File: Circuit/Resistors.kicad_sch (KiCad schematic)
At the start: 23 parts, among them K3 AGQ200A12, K4 AGQ200A12, K5 AGQ200A12, K6 AGQ200A12, K7 AGQ200A12

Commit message: Output job, Revision Box and reorganise
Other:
- company: Harry and Yuki - EEE3 Instrumentation -> Harry Hill and Yuki Hoshino
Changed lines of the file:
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@@
 	(title_block
 		(title "Resistor Selector")
-		(date "2026-03-02")
+		(date "2026-05-02")
 		(rev "1.0")
-		(company "Harry and Yuki - EEE3 Instrumentation")
+		(company "Harry Hill and Yuki Hoshino")
+		(comment 1 "LCR Meter")
 	)
 	(text "fb=100k\n\n"

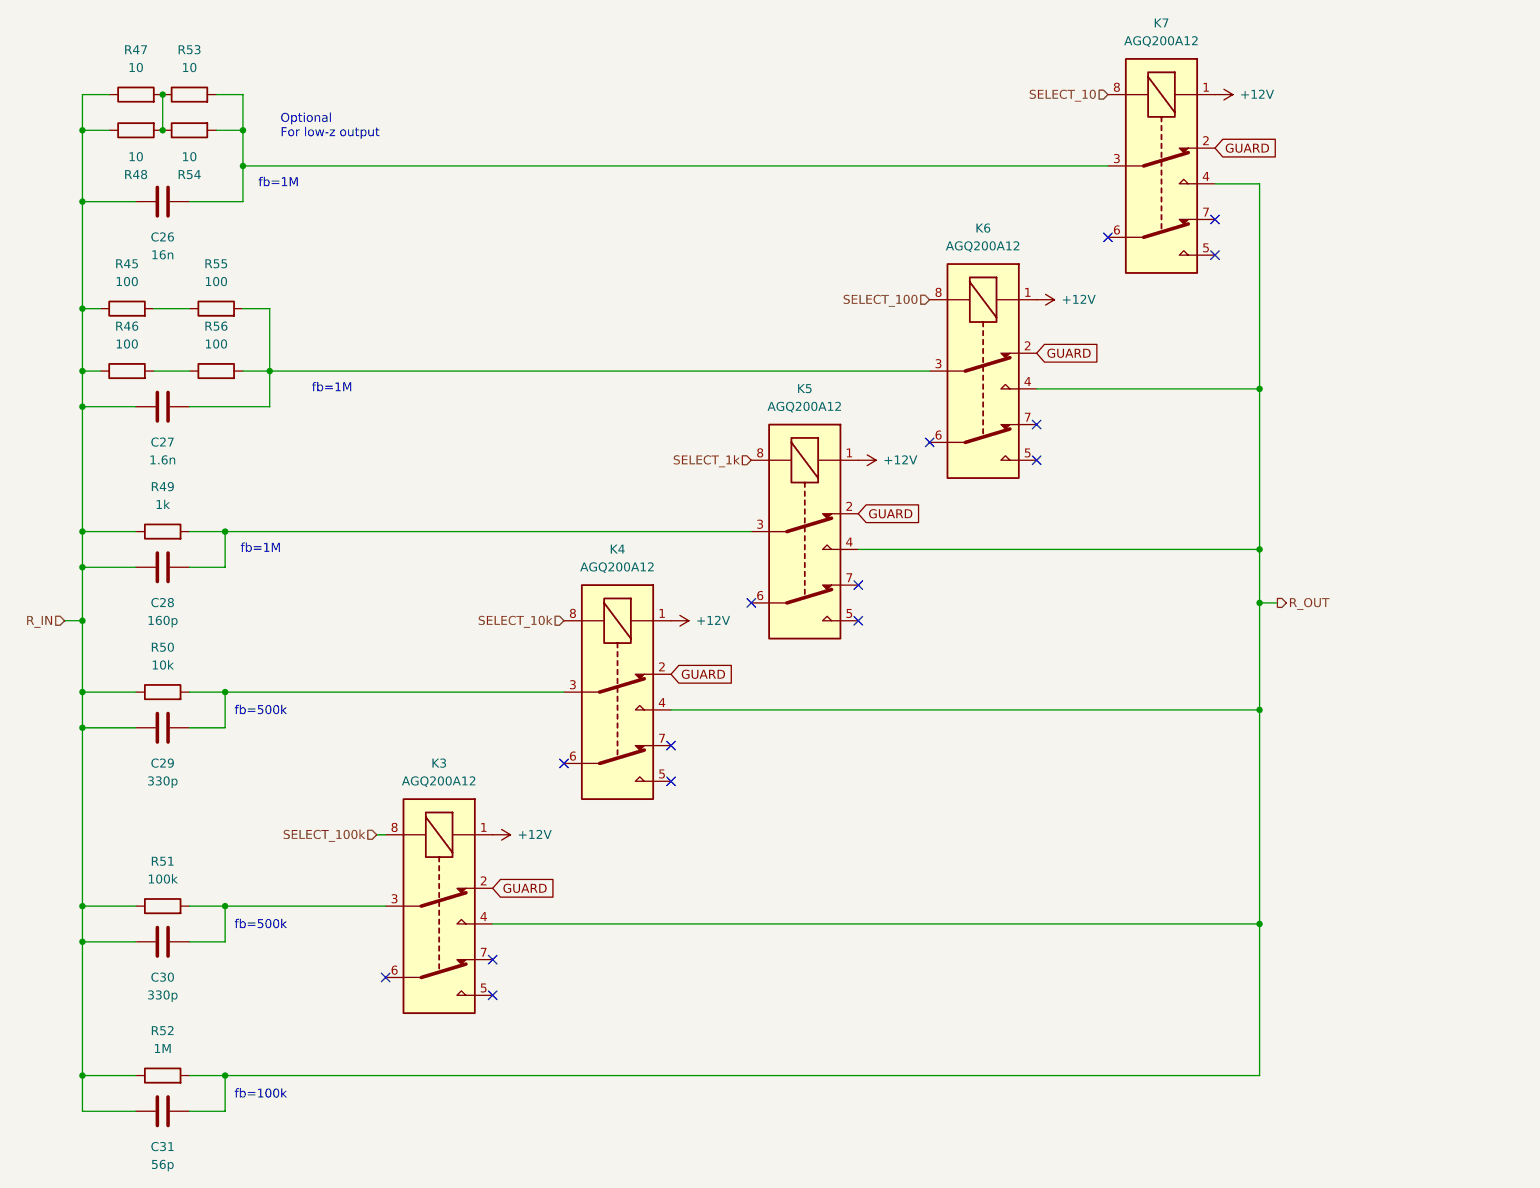
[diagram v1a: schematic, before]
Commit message: Input Protection Second Attempt
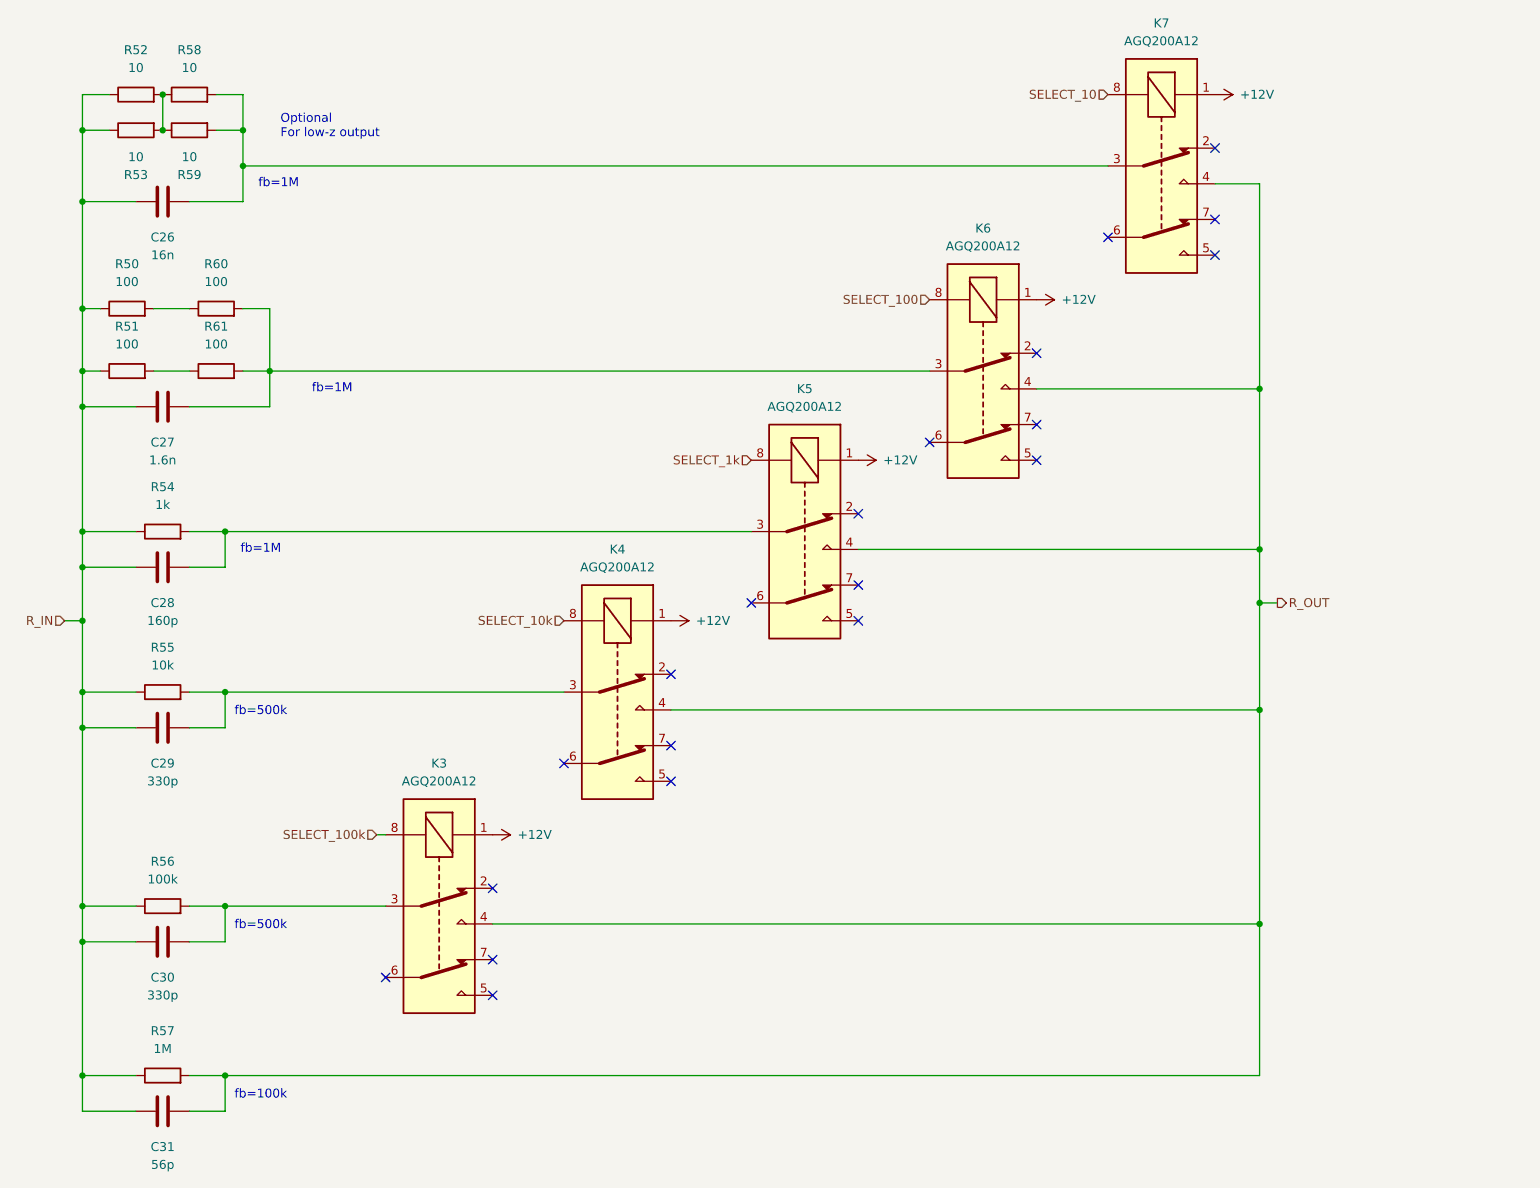
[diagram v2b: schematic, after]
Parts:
- renumbered R45 to R50, R46 to R51, R47 to R52, R48 to R53, R49 to R54, R50 to R55, R51 to R56, R52 to R57, R53 to R58, R54 to R59, R55 to R60, R56 to R61
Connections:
- removed net GUARD: K3.2, K4.2, K5.2, K6.2, K7.2
- no-connect marks 15 -> 20
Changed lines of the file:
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@@
 		(title "Resistor Selector")
 		(date "2026-05-02")
-		(rev "1.0")
+		(rev "0.1")
 		(company "Harry Hill and Yuki Hoshino")
 		(comment 1 "LCR Meter")
@@
 	)
 	(no_connect
+		(at 90.17 137.16)
+	)
+	(no_connect
 		(at 142.24 93.98)
 	)
@@
 	)
 	(no_connect
+		(at 142.24 83.82)
+	)
+	(no_connect
 		(at 167.64 76.2)
 	)
@@
 	)
 	(no_connect
+		(at 167.64 60.96)
+	)
+	(no_connect
 		(at 167.64 71.12)
 	)
@@
 	)
 	(no_connect
+		(at 193.04 31.75)
+	)
+	(no_connect
 		(at 177.8 44.45)
 	)
+	(no_connect
+		(at 115.57 106.68)
+	)
 	(wire
 		(pts
@@
 		)
 	)
-	(global_label "GUARD"
-		(shape input)
-		(at 115.57 106.68 0)
-		(fields_autoplaced yes)
-		(effects
-			(font
-				(size 1.27 1.27)
-			)
-			(justify left)
-		)
-		(property "Intersheetrefs" "${INTERSHEET_REFS}"
-			(at 124.7843 106.68 0)
-			(effects
-				(font
-					(size 1.27 1.27)
-				)
-				(justify left)
-				(hide yes)
-			)
-		)
-	)
-	(global_label "GUARD"
-		(shape input)
-		(at 142.24 83.82 0)
-		(fields_autoplaced yes)
-		(effects
-			(font
-				(size 1.27 1.27)
-			)
-			(justify left)
-		)
-		(property "Intersheetrefs" "${INTERSHEET_REFS}"
-			(at 151.4543 83.82 0)
-			(effects
-				(font
-					(size 1.27 1.27)
-				)
-				(justify left)
-				(hide yes)
-			)
-		)
-	)
-	(global_label "GUARD"
-		(shape input)
-		(at 167.64 60.96 0)
-		(fields_autoplaced yes)
-		(effects
-			(font
-				(size 1.27 1.27)
-			)
-			(justify left)
-		)
-		(property "Intersheetrefs" "${INTERSHEET_REFS}"
-			(at 176.8543 60.96 0)
-			(effects
-				(font
-					(size 1.27 1.27)
-				)
-				(justify left)
-				(hide yes)
-			)
-		)
-	)
-	(global_label "GUARD"
-		(shape input)
-		(at 193.04 31.75 0)
-		(fields_autoplaced yes)
-		(effects
-			(font
-				(size 1.27 1.27)
-			)
-			(justify left)
-		)
-		(property "Intersheetrefs" "${INTERSHEET_REFS}"
-			(at 202.2543 31.75 0)
-			(effects
-				(font
-					(size 1.27 1.27)
-				)
-				(justify left)
-				(hide yes)
-			)
-		)
-	)
-	(global_label "GUARD"
-		(shape input)
-		(at 90.17 137.16 0)
-		(fields_autoplaced yes)
-		(effects
-			(font
-				(size 1.27 1.27)
-			)
-			(justify left)
-		)
-		(property "Intersheetrefs" "${INTERSHEET_REFS}"
-			(at 99.3843 137.16 0)
-			(effects
-				(font
-					(size 1.27 1.27)
-				)
-				(justify left)
-				(hide yes)
-			)
-		)
-	)
 	(hierarchical_label "SELECT_10k"
 		(shape input)
@@
 		(dnp no)
 		(fields_autoplaced yes)
-		(property "Reference" "R49"
+		(property "Reference" "R54"
 			(at 43.18 80.01 90)
 			(effects
@@
 			(project "Main Board"
 				(path "/20aae4b7-3fb8-4924-82e8-1e7a29a313f8/6b7fef71-3444-4c8f-b2e2-502774ba9b51/2542314c-0b08-493b-856b-65d680d18812"
-					(reference "R49")
+					(reference "R54")
 					(unit 1)
 				)
@@
 		(dnp no)
 		(fields_autoplaced yes)
-		(property "Reference" "R47"
+		(property "Reference" "R52"
 			(at 39.37 17.78 90)
 			(effects
@@
 			(project "Main Board"
 				(path "/20aae4b7-3fb8-4924-82e8-1e7a29a313f8/6b7fef71-3444-4c8f-b2e2-502774ba9b51/2542314c-0b08-493b-856b-65d680d18812"
-					(reference "R47")
+					(reference "R52")
 					(unit 1)
 				)
@@
 		(on_board yes)
 		(dnp no)
-		(property "Reference" "#PWR087"
+		(property "Reference" "#PWR090"
 			(at 111.76 99.06 0)
 			(effects
@@
 			(project "Main Board"
 				(path "/20aae4b7-3fb8-4924-82e8-1e7a29a313f8/6b7fef71-3444-4c8f-b2e2-502774ba9b51/2542314c-0b08-493b-856b-65d680d18812"
-					(reference "#PWR087")
+					(reference "#PWR090")
 					(unit 1)
 				)
@@
 		(on_board yes)
 		(dnp no)
-		(property "Reference" "R54"
+		(property "Reference" "R59"
 			(at 46.99 35.56 90)
 			(effects
@@
 			(project "Main Board"
 				(path "/20aae4b7-3fb8-4924-82e8-1e7a29a313f8/6b7fef71-3444-4c8f-b2e2-502774ba9b51/2542314c-0b08-493b-856b-65d680d18812"
-					(reference "R54")
+					(reference "R59")
 					(unit 1)
 				)
@@
 		(on_board yes)
 		(dnp no)
-		(property "Reference" "R56"
+		(property "Reference" "R61"
 			(at 50.8 57.15 90)
 			(effects
@@
 			(project "Main Board"
 				(path "/20aae4b7-3fb8-4924-82e8-1e7a29a313f8/6b7fef71-3444-4c8f-b2e2-502774ba9b51/2542314c-0b08-493b-856b-65d680d18812"
-					(reference "R56")
+					(reference "R61")
 					(unit 1)
 				)
@@
 		(on_board yes)
 		(dnp no)
-		(property "Reference" "#PWR086"
+		(property "Reference" "#PWR089"
 			(at 86.36 129.54 0)
 			(effects
@@
 			(project "Main Board"
 				(path "/20aae4b7-3fb8-4924-82e8-1e7a29a313f8/6b7fef71-3444-4c8f-b2e2-502774ba9b51/2542314c-0b08-493b-856b-65d680d18812"
-					(reference "#PWR086")
+					(reference "#PWR089")
 					(unit 1)
 				)
@@
 		(on_board yes)
 		(dnp no)
-		(property "Reference" "#PWR088"
+		(property "Reference" "#PWR091"
 			(at 138.43 76.2 0)
 			(effects
@@
 			(project "Main Board"
 				(path "/20aae4b7-3fb8-4924-82e8-1e7a29a313f8/6b7fef71-3444-4c8f-b2e2-502774ba9b51/2542314c-0b08-493b-856b-65d680d18812"
-					(reference "#PWR088")
+					(reference "#PWR091")
 					(unit 1)
 				)
@@
 		(dnp no)
 		(fields_autoplaced yes)
-		(property "Reference" "R53"
+		(property "Reference" "R58"
 			(at 46.99 17.78 90)
 			(effects
@@
 			(project "Main Board"
 				(path "/20aae4b7-3fb8-4924-82e8-1e7a29a313f8/6b7fef71-3444-4c8f-b2e2-502774ba9b51/2542314c-0b08-493b-856b-65d680d18812"
-					(reference "R53")
+					(reference "R58")
 					(unit 1)
 				)
@@
 		(on_board yes)
 		(dnp no)
-		(property "Reference" "#PWR090"
+		(property "Reference" "#PWR093"
 			(at 189.23 24.13 0)
 			(effects
@@
 			(project "Main Board"
 				(path "/20aae4b7-3fb8-4924-82e8-1e7a29a313f8/6b7fef71-3444-4c8f-b2e2-502774ba9b51/2542314c-0b08-493b-856b-65d680d18812"
-					(reference "#PWR090")
+					(reference "#PWR093")
 					(unit 1)
 				)
@@
 		(dnp no)
 		(fields_autoplaced yes)
-		(property "Reference" "R51"
+		(property "Reference" "R56"
 			(at 43.18 133.35 90)
 			(effects
@@
 			(project "Main Board"
 				(path "/20aae4b7-3fb8-4924-82e8-1e7a29a313f8/6b7fef71-3444-4c8f-b2e2-502774ba9b51/2542314c-0b08-493b-856b-65d680d18812"
-					(reference "R51")
+					(reference "R56")
 					(unit 1)
 				)
@@
 		(on_board yes)
 		(dnp no)
-		(property "Reference" "R48"
+		(property "Reference" "R53"
 			(at 39.37 35.56 90)
 			(effects
@@
 			(project "Main Board"
 				(path "/20aae4b7-3fb8-4924-82e8-1e7a29a313f8/6b7fef71-3444-4c8f-b2e2-502774ba9b51/2542314c-0b08-493b-856b-65d680d18812"
-					(reference "R48")
+					(reference "R53")
 					(unit 1)
 				)
@@
 		(on_board yes)
 		(dnp no)
-		(property "Reference" "R55"
+		(property "Reference" "R60"
 			(at 50.8 48.26 90)
 			(effects
@@
 			(project "Main Board"
 				(path "/20aae4b7-3fb8-4924-82e8-1e7a29a313f8/6b7fef71-3444-4c8f-b2e2-502774ba9b51/2542314c-0b08-493b-856b-65d680d18812"
-					(reference "R55")
+					(reference "R60")
 					(unit 1)
 				)
@@
 		(on_board yes)
 		(dnp no)
-		(property "Reference" "R45"
+		(property "Reference" "R50"
 			(at 38.1 48.26 90)
 			(effects
@@
 			(project "Main Board"
 				(path "/20aae4b7-3fb8-4924-82e8-1e7a29a313f8/6b7fef71-3444-4c8f-b2e2-502774ba9b51/2542314c-0b08-493b-856b-65d680d18812"
-					(reference "R45")
+					(reference "R50")
 					(unit 1)
 				)
@@
 		(on_board yes)
 		(dnp no)
-		(property "Reference" "#PWR089"
+		(property "Reference" "#PWR092"
 			(at 163.83 53.34 0)
 			(effects
@@
 			(project "Main Board"
 				(path "/20aae4b7-3fb8-4924-82e8-1e7a29a313f8/6b7fef71-3444-4c8f-b2e2-502774ba9b51/2542314c-0b08-493b-856b-65d680d18812"
-					(reference "#PWR089")
+					(reference "#PWR092")
 					(unit 1)
 				)
@@
 		(on_board yes)
 		(dnp no)
-		(property "Reference" "R46"
+		(property "Reference" "R51"
 			(at 38.1 57.15 90)
 			(effects
@@
 			(project "Main Board"
 				(path "/20aae4b7-3fb8-4924-82e8-1e7a29a313f8/6b7fef71-3444-4c8f-b2e2-502774ba9b51/2542314c-0b08-493b-856b-65d680d18812"
-					(reference "R46")
+					(reference "R51")
 					(unit 1)
 				)
@@
 		(dnp no)
 		(fields_autoplaced yes)
-		(property "Reference" "R50"
+		(property "Reference" "R55"
 			(at 43.18 102.87 90)
 			(effects
@@
 			(project "Main Board"
 				(path "/20aae4b7-3fb8-4924-82e8-1e7a29a313f8/6b7fef71-3444-4c8f-b2e2-502774ba9b51/2542314c-0b08-493b-856b-65d680d18812"
-					(reference "R50")
+					(reference "R55")
 					(unit 1)
 				)
@@
 		(on_board yes)
 		(dnp no)
-		(property "Reference" "R52"
+		(property "Reference" "R57"
 			(at 43.18 157.48 90)
 			(effects
@@
 			(project "Main Board"
 				(path "/20aae4b7-3fb8-4924-82e8-1e7a29a313f8/6b7fef71-3444-4c8f-b2e2-502774ba9b51/2542314c-0b08-493b-856b-65d680d18812"
-					(reference "R52")
+					(reference "R57")
 					(unit 1)
 				)

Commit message: New Resistor Selection Circuit
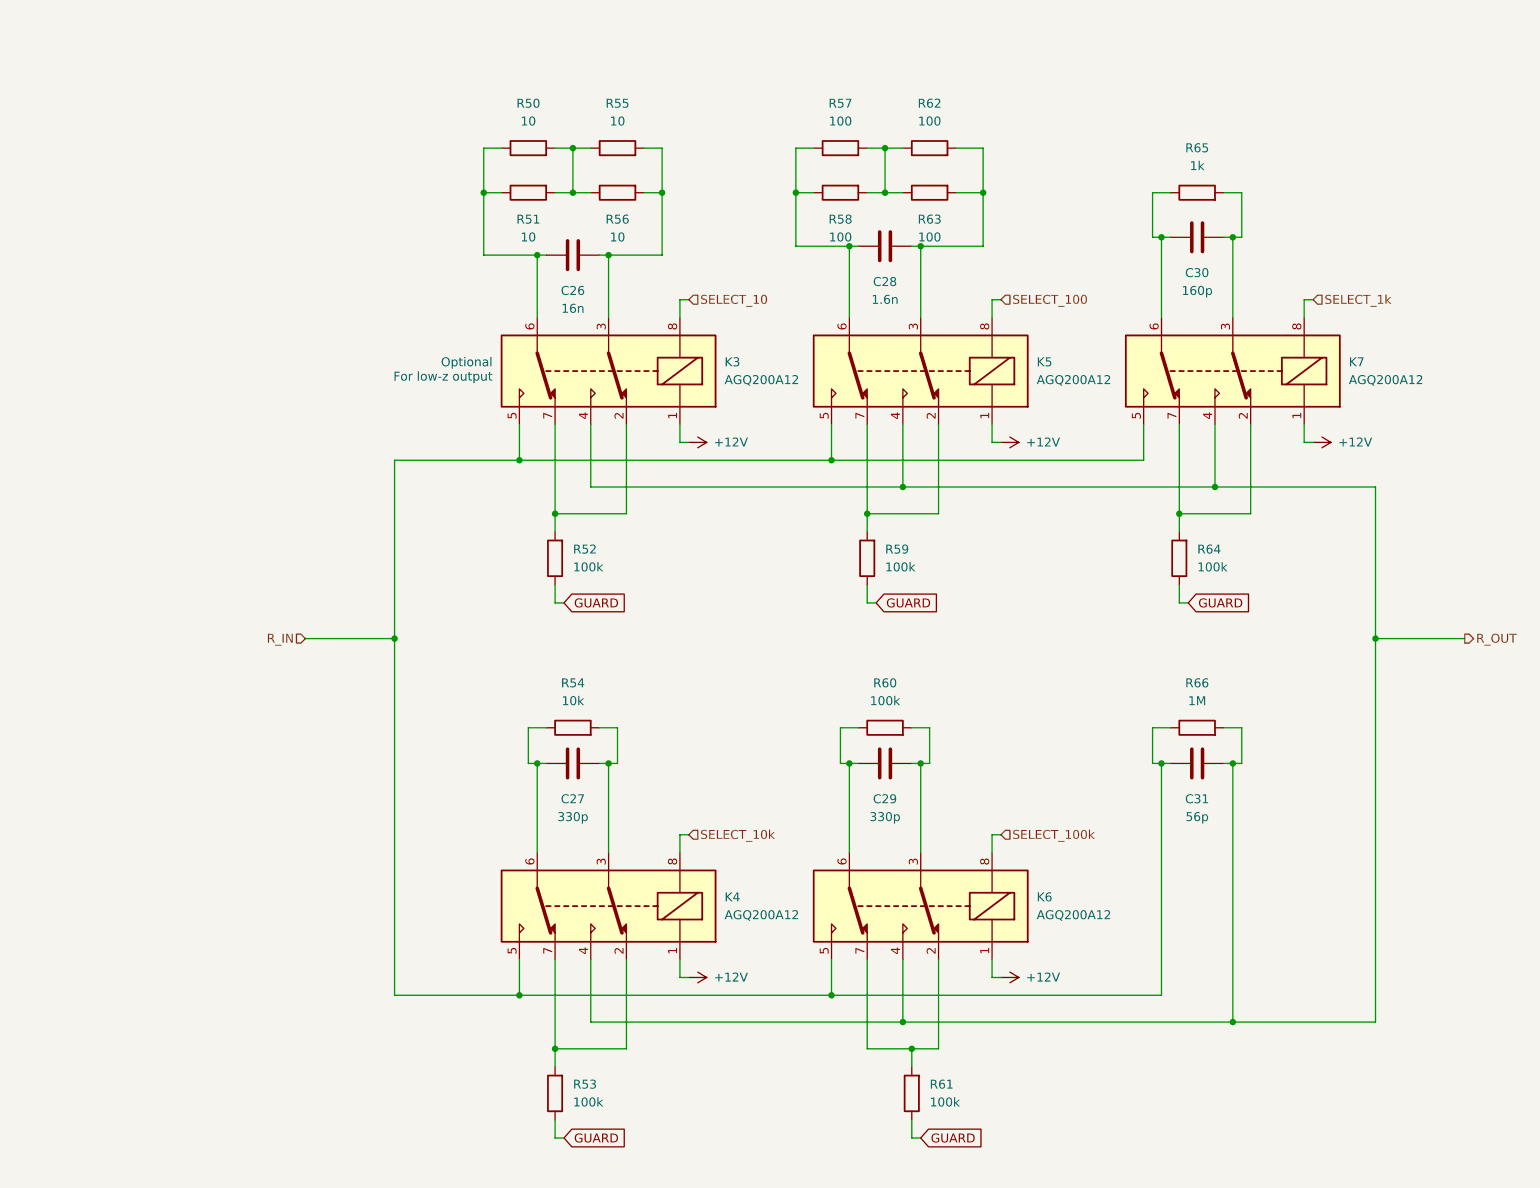
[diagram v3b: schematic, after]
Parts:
- added R52, R53, R59, R61, R64: 100k, Resistor_SMD:R_0805_2012Metric, symbol Device:R
- renumbered C29 to C27, C27 to C28, C30 to C29, C28 to C30, K7 to K3, K6 to K5, K3 to K6, K5 to K7, R52 to R50, R53 to R51, R55 to R54, R58 to R55, R59 to R56, R50 to R57, R51 to R58, R56 to R60, R60 to R62, R61 to R63, R54 to R65, R57 to R66
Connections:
- net R_IN: now also K3.5, K4.5, K5.5, K6.5, K7.5; no longer C26.1, C27.1, C28.1, C29.1, C30.1, R50.1, R51.1, R54.1, R57.1, R58.1, R60.1, R65.1
- net at R58.2, R63.1: now also R57.2, R62.1
- net at K5.2: now also K5.7, R59.2
- net at K5.6: now also C28.1, R57.1, R58.1
- net at K6.2: now also K6.7, R61.2
- net at K6.6: now also C29.1, R60.1
- net at K3.2: now also K3.7, R52.2
- net at K3.6: now also C26.1, R50.1, R51.1
- net at K4.2: now also K4.7, R53.2
- net at K4.6: now also C27.1, R54.1
- net at K7.2: now also K7.7, R64.2
- net at K7.6: now also C30.1, R65.1
- new net GUARD: R52.1, R53.1, R59.1, R61.1, R64.1
- no-connect marks 20 -> 0
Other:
- note removed: "fb=100k"
- note removed: "fb=1M"
- note removed: "fb=500k"
- moved on the sheet: C26, C27, C28, C29, C30, C31, K3, K4, K5, K6, K7, R50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
